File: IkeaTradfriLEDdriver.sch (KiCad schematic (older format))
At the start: 15 parts, among them J1 input, J2 PWM, J3 LED strip, Q1 BUZ11, U1 LM741

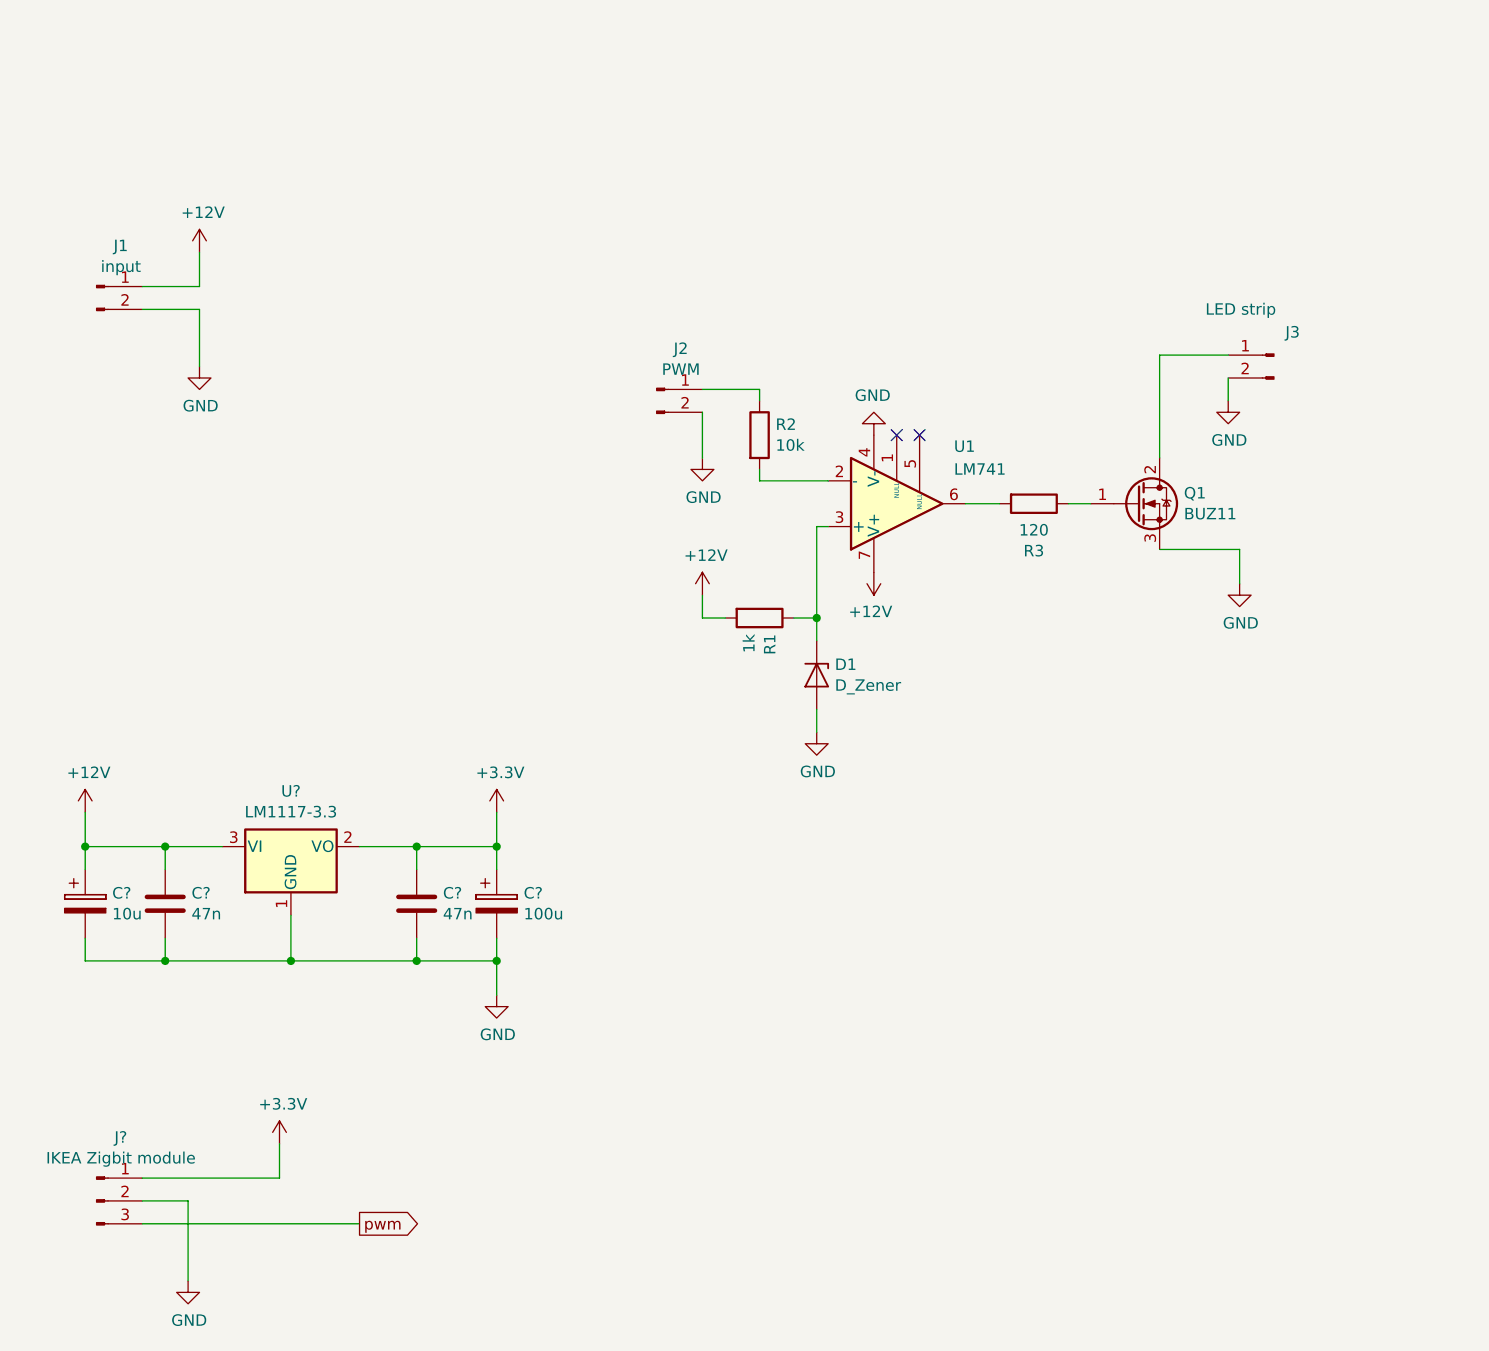
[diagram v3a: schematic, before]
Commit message: Dodelane schema Prirazena pouzdra Vytvoreny netlist Vygenerovana deska
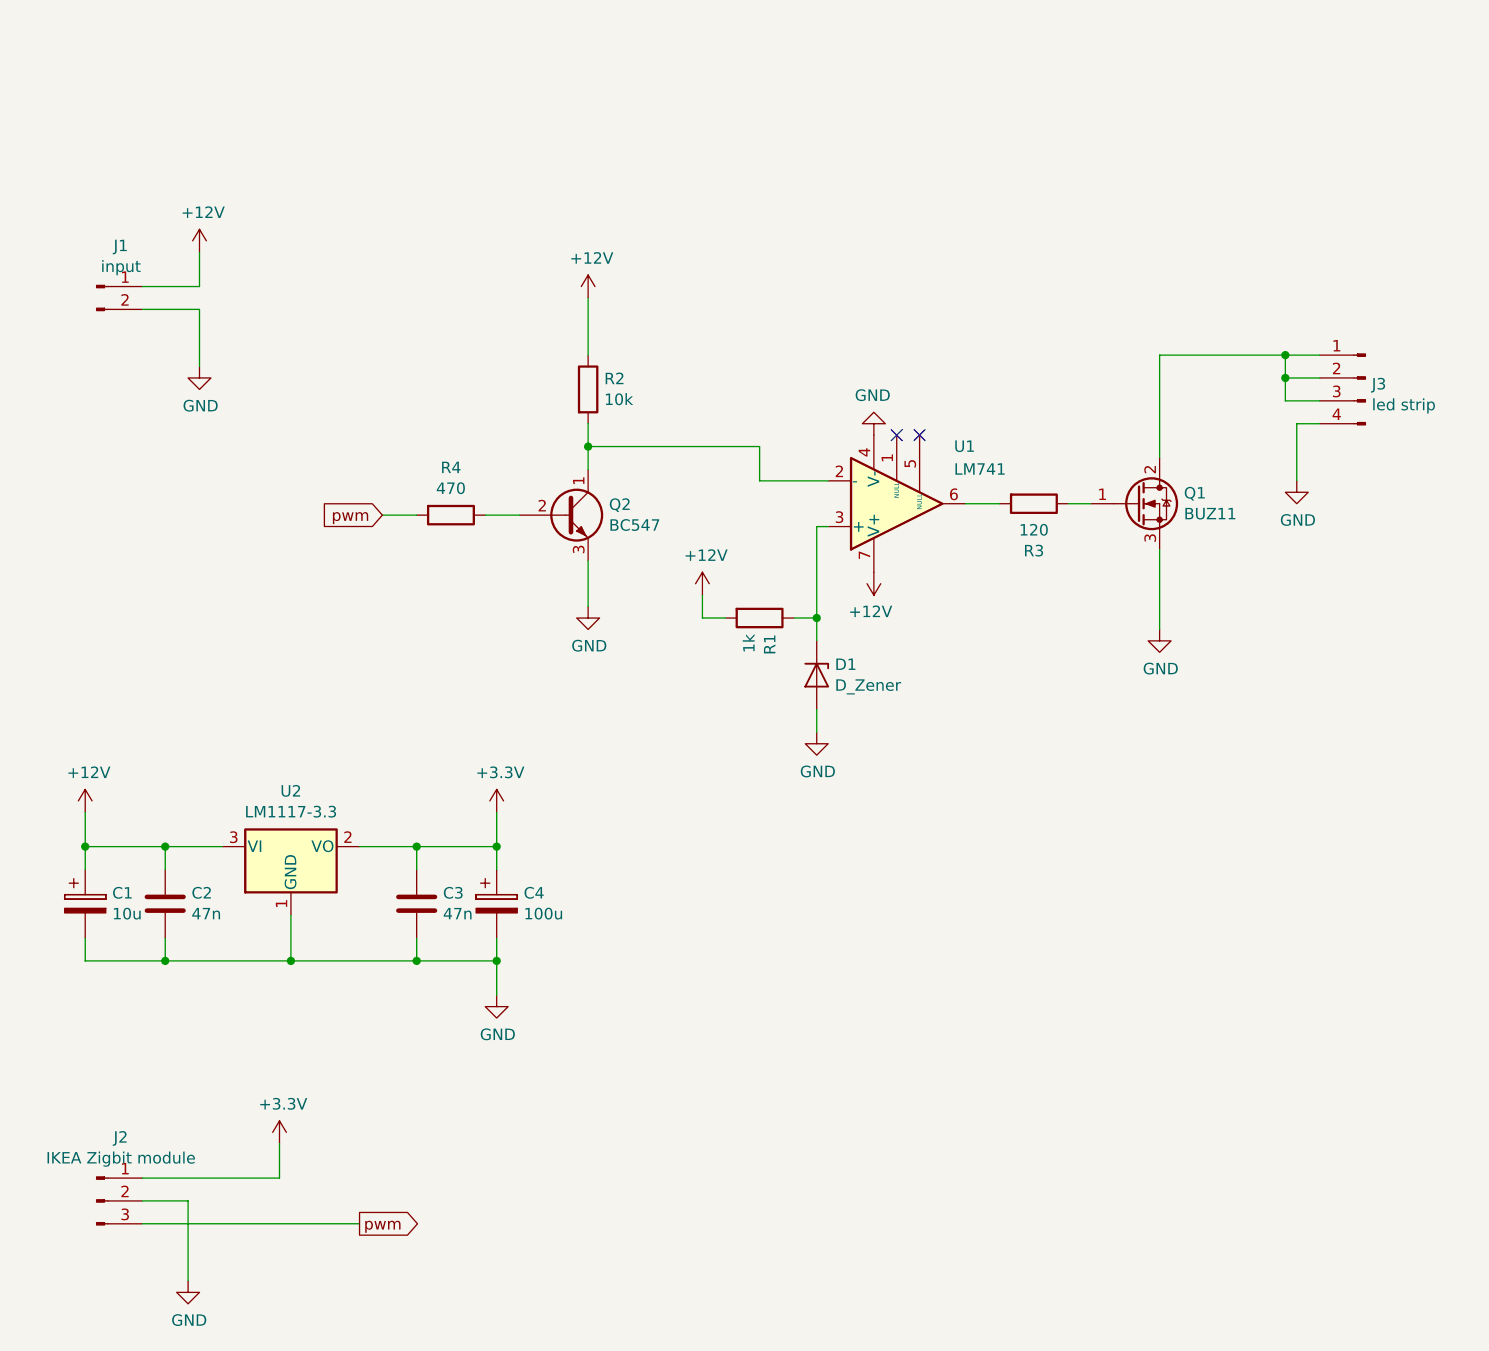
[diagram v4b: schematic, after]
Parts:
- removed J2: PWM, Connector_Wire:SolderWirePad_1x02_P5.08mm_Drill1.5mm, symbol Connector:Conn_01x02_Male
- removed J3: LED strip, Connector_Wire:SolderWirePad_1x02_P5.08mm_Drill1.5mm, symbol Connector:Conn_01x02_Male
- added J3: led strip, Connector_PinHeader_2.54mm:PinHeader_1x04_P2.54mm_Horizontal, symbol Connector:Conn_01x04_Male
- added Q2: BC547, Package_TO_SOT_THT:TO-92_Inline, symbol Transistor_BJT:BC547
- added R4: 470, Resistor_THT:R_Axial_DIN0204_L3.6mm_D1.6mm_P7.62mm_Horizontal, symbol Device:R
- C1: renamed from C?; footprint (none) -> Capacitor_THT:CP_Radial_D5.0mm_P2.50mm
- C2, C3: renamed from C?; footprint (none) -> Capacitor_THT:C_Rect_L7.0mm_W2.0mm_P5.00mm
- C4: renamed from C?; footprint (none) -> Capacitor_THT:CP_Radial_D8.0mm_P5.00mm
- U2: renamed from U?; footprint (none) -> Package_TO_SOT_THT:TO-220-3_Vertical
- gave numbers to parts that had none: 1
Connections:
- net +12V: now also R2.1
- net GND: now also J3.4 (Pin_4), Q2.3 (E)
- net pwm: now also R4.2
- net at Q1.2 (D): now also J3.1 (Pin_1), J3.2 (Pin_2), J3.3 (Pin_3)
- net at R2.2, U1.2 (-): now also Q2.1 (C)
- new net: Q2.2 (B), R4.1
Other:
- moved on the sheet: R2
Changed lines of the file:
@@
 L Device:R R2
 U 1 1 5C6C17A3
-P 4000 2700
-F 0 "R2" H 4070 2746 50  0000 L CNN
-F 1 "10k" H 4070 2655 50  0000 L CNN
-F 2 "Resistor_THT:R_Axial_DIN0309_L9.0mm_D3.2mm_P12.70mm_Horizontal" V 3930 2700 50  0001 C CNN
-F 3 "~" H 4000 2700 50  0001 C CNN
-	1    4000 2700
+P 3250 2500
+F 0 "R2" H 3320 2546 50  0000 L CNN
+F 1 "10k" H 3320 2455 50  0000 L CNN
+F 2 "Resistor_THT:R_Axial_DIN0309_L9.0mm_D3.2mm_P12.70mm_Horizontal" V 3180 2500 50  0001 C CNN
+F 3 "~" H 3250 2500 50  0001 C CNN
+	1    3250 2500
 	1    0    0    -1
 $EndComp
@@
 L power:GND #PWR0103
 U 1 1 5C6C56E4
-P 6100 3350
-F 0 "#PWR0103" H 6100 3100 50  0001 C CNN
-F 1 "GND" H 6105 3177 50  0000 C CNN
-F 2 "" H 6100 3350 50  0001 C CNN
-F 3 "" H 6100 3350 50  0001 C CNN
-	1    6100 3350
-	1    0    0    -1
-$EndComp
-Wire Wire Line
-	6100 3350 6100 3200
+P 5750 3550
+F 0 "#PWR0103" H 5750 3300 50  0001 C CNN
+F 1 "GND" H 5755 3377 50  0000 C CNN
+F 2 "" H 5750 3550 50  0001 C CNN
+F 3 "" H 5750 3550 50  0001 C CNN
+	1    5750 3550
+	1    0    0    -1
+$EndComp
 Wire Wire Line
 	4000 2900 4300 2900
-$Comp
-L Connector:Conn_01x02_Male J2
-U 1 1 5C6C6B7B
-P 3550 2500
-F 0 "J2" H 3656 2678 50  0000 C CNN
-F 1 "PWM" H 3656 2587 50  0000 C CNN
-F 2 "Connector_Wire:SolderWirePad_1x02_P5.08mm_Drill1.5mm" H 3550 2500 50  0001 C CNN
-F 3 "~" H 3550 2500 50  0001 C CNN
-	1    3550 2500
-	1    0    0    -1
-$EndComp
-$Comp
-L Connector:Conn_01x02_Male J3
-U 1 1 5C6C6DFD
-P 6250 2350
-F 0 "J3" H 6200 2450 50  0000 R CNN
-F 1 "LED strip" H 6550 2550 50  0000 R CNN
-F 2 "Connector_Wire:SolderWirePad_1x02_P5.08mm_Drill1.5mm" H 6250 2350 50  0001 C CNN
-F 3 "~" H 6250 2350 50  0001 C CNN
-	1    6250 2350
-	-1   0    0    -1
-$EndComp
 $Comp
 L Connector:Conn_01x02_Male J1
@@
 $EndComp
 Wire Wire Line
-	3750 2500 4000 2500
-Wire Wire Line
-	4000 2500 4000 2550
-Wire Wire Line
-	4000 2850 4000 2900
-$Comp
-L power:GND #PWR0104
-U 1 1 5C6C7B70
-P 3750 2800
-F 0 "#PWR0104" H 3750 2550 50  0001 C CNN
-F 1 "GND" H 3755 2627 50  0000 C CNN
-F 2 "" H 3750 2800 50  0001 C CNN
-F 3 "" H 3750 2800 50  0001 C CNN
-	1    3750 2800
-	1    0    0    -1
-$EndComp
-Wire Wire Line
-	3750 2600 3750 2800
-Wire Wire Line
 	4900 3000 5050 3000
 Wire Wire Line
 	5350 3000 5450 3000
 Wire Wire Line
-	5750 3200 6100 3200
-Wire Wire Line
 	5750 2800 5750 2350
-Wire Wire Line
-	5750 2350 6050 2350
 $Comp
 L power:GND #PWR0105
 U 1 1 5C6C8827
-P 6050 2550
-F 0 "#PWR0105" H 6050 2300 50  0001 C CNN
-F 1 "GND" H 6055 2377 50  0000 C CNN
-F 2 "" H 6050 2550 50  0001 C CNN
-F 3 "" H 6050 2550 50  0001 C CNN
-	1    6050 2550
-	1    0    0    -1
-$EndComp
-Wire Wire Line
-	6050 2450 6050 2550
+P 6350 2900
+F 0 "#PWR0105" H 6350 2650 50  0001 C CNN
+F 1 "GND" H 6355 2727 50  0000 C CNN
+F 2 "" H 6350 2900 50  0001 C CNN
+F 3 "" H 6350 2900 50  0001 C CNN
+	1    6350 2900
+	1    0    0    -1
+$EndComp
 $Comp
 L power:GND #PWR0101
@@
 $EndComp
 $Comp
-L Regulator_Linear:LM1117-3.3 U?
+L Regulator_Linear:LM1117-3.3 U2
 U 1 1 5C75B3A7
 P 1950 4500
-F 0 "U?" H 1950 4742 50  0000 C CNN
+F 0 "U2" H 1950 4742 50  0000 C CNN
 F 1 "LM1117-3.3" H 1950 4651 50  0000 C CNN
-F 2 "" H 1950 4500 50  0001 C CNN
+F 2 "Package_TO_SOT_THT:TO-220-3_Vertical" H 1950 4500 50  0001 C CNN
 F 3 "http://www.ti.com/lit/ds/symlink/lm1117.pdf" H 1950 4500 50  0001 C CNN
 	1    1950 4500
@@
 $EndComp
 $Comp
-L power:+12V #PWR?
+L power:+12V #PWR0104
 U 1 1 5C75B47A
 P 1050 4350
-F 0 "#PWR?" H 1050 4200 50  0001 C CNN
+F 0 "#PWR0104" H 1050 4200 50  0001 C CNN
 F 1 "+12V" H 1065 4523 50  0000 C CNN
 F 2 "" H 1050 4350 50  0001 C CNN
@@
 $EndComp
 $Comp
-L power:+3.3V #PWR?
+L power:+3.3V #PWR0110
 U 1 1 5C75B500
 P 2850 4350
-F 0 "#PWR?" H 2850 4200 50  0001 C CNN
+F 0 "#PWR0110" H 2850 4200 50  0001 C CNN
 F 1 "+3.3V" H 2865 4523 50  0000 C CNN
 F 2 "" H 2850 4350 50  0001 C CNN
@@
 $EndComp
 $Comp
-L Device:C C?
+L Device:C C2
 U 1 1 5C75B55C
 P 1400 4750
-F 0 "C?" H 1515 4796 50  0000 L CNN
+F 0 "C2" H 1515 4796 50  0000 L CNN
 F 1 "47n" H 1515 4705 50  0000 L CNN
-F 2 "" H 1438 4600 50  0001 C CNN
+F 2 "Capacitor_THT:C_Rect_L7.0mm_W2.0mm_P5.00mm" H 1438 4600 50  0001 C CNN
 F 3 "~" H 1400 4750 50  0001 C CNN
 	1    1400 4750
@@
 $EndComp
 $Comp
-L Device:C C?
+L Device:C C3
 U 1 1 5C75B5D1
 P 2500 4750
-F 0 "C?" H 2615 4796 50  0000 L CNN
+F 0 "C3" H 2615 4796 50  0000 L CNN
 F 1 "47n" H 2615 4705 50  0000 L CNN
-F 2 "" H 2538 4600 50  0001 C CNN
+F 2 "Capacitor_THT:C_Rect_L7.0mm_W2.0mm_P5.00mm" H 2538 4600 50  0001 C CNN
 F 3 "~" H 2500 4750 50  0001 C CNN
 	1    2500 4750
@@
 $EndComp
 $Comp
-L Device:CP C?
+L Device:CP C1
 U 1 1 5C75B961
 P 1050 4750
-F 0 "C?" H 1168 4796 50  0000 L CNN
+F 0 "C1" H 1168 4796 50  0000 L CNN
 F 1 "10u" H 1168 4705 50  0000 L CNN
-F 2 "" H 1088 4600 50  0001 C CNN
+F 2 "Capacitor_THT:CP_Radial_D5.0mm_P2.50mm" H 1088 4600 50  0001 C CNN
 F 3 "~" H 1050 4750 50  0001 C CNN
 	1    1050 4750
@@
 $EndComp
 $Comp
-L Device:CP C?
+L Device:CP C4
 U 1 1 5C75BADC
 P 2850 4750
-F 0 "C?" H 2968 4796 50  0000 L CNN
+F 0 "C4" H 2968 4796 50  0000 L CNN
 F 1 "100u" H 2968 4705 50  0000 L CNN
-F 2 "" H 2888 4600 50  0001 C CNN
+F 2 "Capacitor_THT:CP_Radial_D8.0mm_P5.00mm" H 2888 4600 50  0001 C CNN
 F 3 "~" H 2850 4750 50  0001 C CNN
 	1    2850 4750
@@
 	1400 5000 1950 5000
 $Comp
-L power:GND #PWR?
+L power:GND #PWR0111
 U 1 1 5C75EF0F
 P 2850 5150
-F 0 "#PWR?" H 2850 4900 50  0001 C CNN
+F 0 "#PWR0111" H 2850 4900 50  0001 C CNN
 F 1 "GND" H 2855 4977 50  0000 C CNN
 F 2 "" H 2850 5150 50  0001 C CNN
@@
 Connection ~ 2850 5000
 $Comp
-L Connector:Conn_01x03_Male J?
+L Connector:Conn_01x03_Male J2
 U 1 1 5C761CEC
 P 1100 6050
-F 0 "J?" H 1206 6328 50  0000 C CNN
+F 0 "J2" H 1206 6328 50  0000 C CNN
 F 1 "IKEA Zigbit module" H 1206 6237 50  0000 C CNN
 F 2 "Connector_PinHeader_1.27mm:PinHeader_1x03_P1.27mm_Vertical" H 1100 6050 50  0001 C CNN
@@
 $EndComp
 $Comp
-L power:GND #PWR?
+L power:GND #PWR0112
 U 1 1 5C76258E
 P 1500 6400
-F 0 "#PWR?" H 1500 6150 50  0001 C CNN
+F 0 "#PWR0112" H 1500 6150 50  0001 C CNN
 F 1 "GND" H 1505 6227 50  0000 C CNN
 F 2 "" H 1500 6400 50  0001 C CNN
@@
 $EndComp
 $Comp
-L power:+3.3V #PWR?
+L power:+3.3V #PWR0113
 U 1 1 5C762623
 P 1900 5800
-F 0 "#PWR?" H 1900 5650 50  0001 C CNN
+F 0 "#PWR0113" H 1900 5650 50  0001 C CNN
 F 1 "+3.3V" H 1915 5973 50  0000 C CNN
 F 2 "" H 1900 5800 50  0001 C CNN
@@
 Wire Wire Line
 	1300 6150 2250 6150
+$Comp
+L Transistor_BJT:BC547 Q2
+U 1 1 5C76726F
+P 3150 3050
+F 0 "Q2" H 3341 3096 50  0000 L CNN
+F 1 "BC547" H 3341 3005 50  0000 L CNN
+F 2 "Package_TO_SOT_THT:TO-92_Inline" H 3350 2975 50  0001 L CIN
+F 3 "http://www.fairchildsemi.com/ds/BC/BC547.pdf" H 3150 3050 50  0001 L CNN
+	1    3150 3050
+	1    0    0    -1
+$EndComp
+$Comp
+L power:+12V #PWR0114
+U 1 1 5C76746B
+P 3250 2100
+F 0 "#PWR0114" H 3250 1950 50  0001 C CNN
+F 1 "+12V" H 3265 2273 50  0000 C CNN
+F 2 "" H 3250 2100 50  0001 C CNN
+F 3 "" H 3250 2100 50  0001 C CNN
+	1    3250 2100
+	1    0    0    -1
+$EndComp
+Text GLabel 2350 3050 0    50   Input ~ 0
+pwm
+$Comp
+L Device:R R4
+U 1 1 5C76C239
+P 2650 3050
+F 0 "R4" V 2443 3050 50  0000 C CNN
+F 1 "470" V 2534 3050 50  0000 C CNN
+F 2 "Resistor_THT:R_Axial_DIN0204_L3.6mm_D1.6mm_P7.62mm_Horizontal" V 2580 3050 50  0001 C CNN
+F 3 "~" H 2650 3050 50  0001 C CNN
+	1    2650 3050
+	0    1    1    0
+$EndComp
+Wire Wire Line
+	2350 3050 2500 3050
+Wire Wire Line
+	2800 3050 2950 3050
+$Comp
+L power:GND #PWR01
+U 1 1 5C770586
+P 3250 3450
+F 0 "#PWR01" H 3250 3200 50  0001 C CNN
+F 1 "GND" H 3255 3277 50  0000 C CNN
+F 2 "" H 3250 3450 50  0001 C CNN
+F 3 "" H 3250 3450 50  0001 C CNN
+	1    3250 3450
+	1    0    0    -1
+$EndComp
+Wire Wire Line
+	3250 3450 3250 3250
+Wire Wire Line
+	3250 2850 3250 2750
+Wire Wire Line
+	3250 2350 3250 2100
+Wire Wire Line
+	3250 2750 4000 2750
+Wire Wire Line
+	4000 2750 4000 2900
+Connection ~ 3250 2750
+Wire Wire Line
+	3250 2750 3250 2650
+$Comp
+L Connector:Conn_01x04_Male J3
+U 1 1 5C773E4C
+P 6650 2450
+F 0 "J3" H 6622 2423 50  0000 R CNN
+F 1 "led strip" H 6622 2332 50  0000 R CNN
+F 2 "Connector_PinHeader_2.54mm:PinHeader_1x04_P2.54mm_Horizontal" H 6650 2450 50  0001 C CNN
+F 3 "~" H 6650 2450 50  0001 C CNN
+	1    6650 2450
+	-1   0    0    -1
+$EndComp
+Wire Wire Line
+	6450 2650 6350 2650
+Wire Wire Line
+	6350 2650 6350 2900
+Wire Wire Line
+	5750 2350 6300 2350
+Wire Wire Line
+	6450 2450 6300 2450
+Wire Wire Line
+	6300 2450 6300 2350
+Connection ~ 6300 2350
+Wire Wire Line
+	6300 2350 6450 2350
+Wire Wire Line
+	6450 2550 6300 2550
+Wire Wire Line
+	6300 2550 6300 2450
+Connection ~ 6300 2450
+Wire Wire Line
+	5750 3200 5750 3550
 $EndSCHEMATC

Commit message: Provedene opravy na desce
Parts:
- removed J1: input, Connector_Wire:SolderWirePad_1x02_P5.08mm_Drill1.5mm, symbol Connector:Conn_01x02_Male
- added H1: +, MountingHole:MountingHole_2.5mm_Pad, symbol Mechanical:MountingHole_Pad
- added H2: -, MountingHole:MountingHole_2.5mm_Pad, symbol Mechanical:MountingHole_Pad
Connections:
- net +12V: now also H1.1
- net GND: now also H2.1
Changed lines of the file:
@@
 Wire Wire Line
 	4000 2900 4300 2900
-$Comp
-L Connector:Conn_01x02_Male J1
-U 1 1 5C6C6F0A
-P 1100 2050
-F 0 "J1" H 1206 2228 50  0000 C CNN
-F 1 "input" H 1206 2137 50  0000 C CNN
-F 2 "Connector_Wire:SolderWirePad_1x02_P5.08mm_Drill1.5mm" H 1100 2050 50  0001 C CNN
-F 3 "~" H 1100 2050 50  0001 C CNN
-	1    1100 2050
-	1    0    0    -1
-$EndComp
 Wire Wire Line
 	4900 3000 5050 3000
@@
 L power:+12V #PWR0102
 U 1 1 5C7538CD
-P 1550 1900
-F 0 "#PWR0102" H 1550 1750 50  0001 C CNN
-F 1 "+12V" H 1565 2073 50  0000 C CNN
-F 2 "" H 1550 1900 50  0001 C CNN
-F 3 "" H 1550 1900 50  0001 C CNN
-	1    1550 1900
-	1    0    0    -1
-$EndComp
-Wire Wire Line
-	1550 1900 1550 2050
-Wire Wire Line
-	1550 2050 1300 2050
-Wire Wire Line
-	1300 2150 1550 2150
-Wire Wire Line
-	1550 2150 1550 2400
+P 1300 1850
+F 0 "#PWR0102" H 1300 1700 50  0001 C CNN
+F 1 "+12V" H 1315 2023 50  0000 C CNN
+F 2 "" H 1300 1850 50  0001 C CNN
+F 3 "" H 1300 1850 50  0001 C CNN
+	1    1300 1850
+	1    0    0    -1
+$EndComp
 $Comp
 L power:GND #PWR0106
 U 1 1 5C753C9C
-P 1550 2400
-F 0 "#PWR0106" H 1550 2150 50  0001 C CNN
-F 1 "GND" H 1555 2227 50  0000 C CNN
-F 2 "" H 1550 2400 50  0001 C CNN
-F 3 "" H 1550 2400 50  0001 C CNN
-	1    1550 2400
+P 1250 2900
+F 0 "#PWR0106" H 1250 2650 50  0001 C CNN
+F 1 "GND" H 1255 2727 50  0000 C CNN
+F 2 "" H 1250 2900 50  0001 C CNN
+F 3 "" H 1250 2900 50  0001 C CNN
+	1    1250 2900
 	1    0    0    -1
 $EndComp
@@
 Wire Wire Line
 	5750 3200 5750 3550
+$Comp
+L Mechanical:MountingHole_Pad H1
+U 1 1 5C768D8F
+P 1050 2050
+F 0 "H1" V 1287 2055 50  0000 C CNN
+F 1 "+" V 1196 2055 50  0000 C CNN
+F 2 "MountingHole:MountingHole_2.5mm_Pad" H 1050 2050 50  0001 C CNN
+F 3 "~" H 1050 2050 50  0001 C CNN
+	1    1050 2050
+	0    -1   -1   0
+$EndComp
+$Comp
+L Mechanical:MountingHole_Pad H2
+U 1 1 5C768E82
+P 1050 2600
+F 0 "H2" V 1287 2605 50  0000 C CNN
+F 1 "-" V 1196 2605 50  0000 C CNN
+F 2 "MountingHole:MountingHole_2.5mm_Pad" H 1050 2600 50  0001 C CNN
+F 3 "~" H 1050 2600 50  0001 C CNN
+	1    1050 2600
+	0    -1   -1   0
+$EndComp
+Wire Wire Line
+	1300 1850 1300 2050
+Wire Wire Line
+	1300 2050 1150 2050
+Wire Wire Line
+	1150 2600 1250 2600
+Wire Wire Line
+	1250 2600 1250 2900
 $EndSCHEMATC
